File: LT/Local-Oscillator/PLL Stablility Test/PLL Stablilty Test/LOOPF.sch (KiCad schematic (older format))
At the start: 5 parts

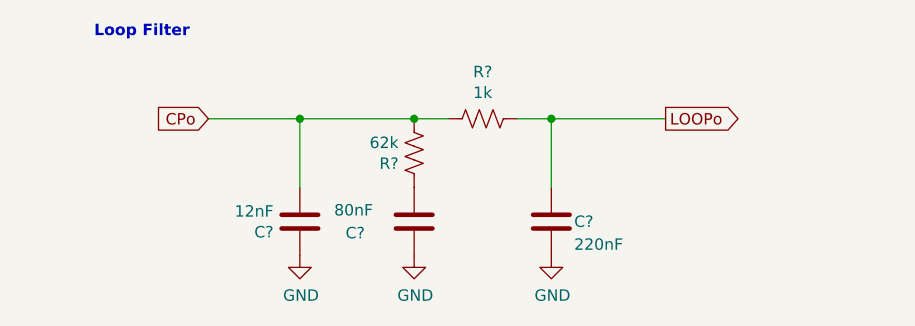
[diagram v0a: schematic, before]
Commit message: completed PLL stability test layour for individual boards
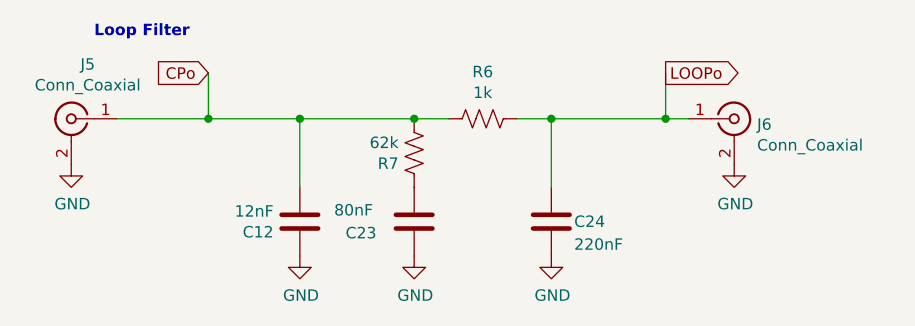
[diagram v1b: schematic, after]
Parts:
- added J5, J6: Conn_Coaxial, Connector_Coaxial:SMA_Molex_73251-1153_EdgeMount_Horizontal, symbol Connector:Conn_Coaxial
- gave numbers to parts that had none: 5
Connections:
- net CPo: now also J5.1 (In)
- net GND: now also J5.2 (Ext), J6.2 (Ext)
- net LOOPo: now also J6.1 (In)
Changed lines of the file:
@@
 AR Path="/5E6F2DE3" Ref="#PWR?"  Part="1"
 AR Path="/5E6E06F1/5E6F2DE3" Ref="#PWR?"  Part="1"
-AR Path="/5E6053F1/5E6F2DE3" Ref="#PWR?"  Part="1"
-F 0 "#PWR?" H 6450 4300 50  0001 C CNN
+AR Path="/5E6053F1/5E6F2DE3" Ref="#PWR0120"  Part="1"
+F 0 "#PWR0120" H 6450 4300 50  0001 C CNN
 F 1 "GND" H 6455 4377 50  0000 C CNN
 F 2 "" H 6450 4550 50  0001 C CNN
@@
 AR Path="/5E6F2DE9" Ref="C?"  Part="1"
 AR Path="/5E6E06F1/5E6F2DE9" Ref="C?"  Part="1"
-AR Path="/5E6053F1/5E6F2DE9" Ref="C?"  Part="1"
-F 0 "C?" H 6550 4400 50  0000 L CNN
+AR Path="/5E6053F1/5E6F2DE9" Ref="C24"  Part="1"
+F 0 "C24" H 6550 4400 50  0000 L CNN
 F 1 "220nF" H 6550 4300 50  0000 L CNN
 F 2 "Capacitor_SMD:C_0805_2012Metric_Pad1.15x1.40mm_HandSolder" H 6488 4250 50  0001 C CNN
@@
 AR Path="/5E6F2DF0" Ref="#PWR?"  Part="1"
 AR Path="/5E6E06F1/5E6F2DF0" Ref="#PWR?"  Part="1"
-AR Path="/5E6053F1/5E6F2DF0" Ref="#PWR?"  Part="1"
-F 0 "#PWR?" H 5850 4300 50  0001 C CNN
+AR Path="/5E6053F1/5E6F2DF0" Ref="#PWR0121"  Part="1"
+F 0 "#PWR0121" H 5850 4300 50  0001 C CNN
 F 1 "GND" H 5855 4377 50  0000 C CNN
 F 2 "" H 5850 4550 50  0001 C CNN
@@
 AR Path="/5E6F2DF7" Ref="C?"  Part="1"
 AR Path="/5E6E06F1/5E6F2DF7" Ref="C?"  Part="1"
-AR Path="/5E6053F1/5E6F2DF7" Ref="C?"  Part="1"
-F 0 "C?" H 5550 4350 50  0000 L CNN
+AR Path="/5E6053F1/5E6F2DF7" Ref="C23"  Part="1"
+F 0 "C23" H 5550 4350 50  0000 L CNN
 F 1 "80nF" H 5500 4450 50  0000 L CNN
 F 2 "Capacitor_SMD:C_0805_2012Metric_Pad1.15x1.40mm_HandSolder" H 5888 4250 50  0001 C CNN
@@
 AR Path="/5E6F2DFD" Ref="#PWR?"  Part="1"
 AR Path="/5E6E06F1/5E6F2DFD" Ref="#PWR?"  Part="1"
-AR Path="/5E6053F1/5E6F2DFD" Ref="#PWR?"  Part="1"
-F 0 "#PWR?" H 5350 4300 50  0001 C CNN
+AR Path="/5E6053F1/5E6F2DFD" Ref="#PWR0122"  Part="1"
+F 0 "#PWR0122" H 5350 4300 50  0001 C CNN
 F 1 "GND" H 5355 4377 50  0000 C CNN
 F 2 "" H 5350 4550 50  0001 C CNN
@@
 AR Path="/5E6F2E04" Ref="C?"  Part="1"
 AR Path="/5E6E06F1/5E6F2E04" Ref="C?"  Part="1"
-AR Path="/5E6053F1/5E6F2E04" Ref="C?"  Part="1"
-F 0 "C?" H 5465 4446 50  0000 L CNN
+AR Path="/5E6053F1/5E6F2E04" Ref="C12"  Part="1"
+F 0 "C12" H 5465 4446 50  0000 L CNN
 F 1 "12nF" H 5465 4355 50  0000 L CNN
 F 2 "Capacitor_SMD:C_0805_2012Metric_Pad1.15x1.40mm_HandSolder" H 5388 4250 50  0001 C CNN
@@
 AR Path="/5E6F2E0B" Ref="R?"  Part="1"
 AR Path="/5E6E06F1/5E6F2E0B" Ref="R?"  Part="1"
-AR Path="/5E6053F1/5E6F2E0B" Ref="R?"  Part="1"
-F 0 "R?" V 5945 3950 50  0000 C CNN
+AR Path="/5E6053F1/5E6F2E0B" Ref="R6"  Part="1"
+F 0 "R6" V 5945 3950 50  0000 C CNN
 F 1 "1k" V 6036 3950 50  0000 C CNN
 F 2 "Resistor_SMD:R_0805_2012Metric_Pad1.15x1.40mm_HandSolder" V 6190 3940 50  0001 C CNN
@@
 AR Path="/5E6F2E11" Ref="R?"  Part="1"
 AR Path="/5E6E06F1/5E6F2E11" Ref="R?"  Part="1"
-AR Path="/5E6053F1/5E6F2E11" Ref="R?"  Part="1"
-F 0 "R?" H 5918 4146 50  0000 L CNN
+AR Path="/5E6053F1/5E6F2E11" Ref="R7"  Part="1"
+F 0 "R7" H 5918 4146 50  0000 L CNN
 F 1 "62k" H 5918 4055 50  0000 L CNN
 F 2 "Resistor_SMD:R_0805_2012Metric_Pad1.15x1.40mm_HandSolder" V 5890 4090 50  0001 C CNN
@@
 Wire Wire Line
 	5850 3950 6000 3950
-Text GLabel 4950 3950 0    50   Input ~ 0
+Text GLabel 4950 3750 0    50   Input ~ 0
 CPo
-Text GLabel 6950 3950 2    50   Output ~ 0
+Text GLabel 6950 3750 2    50   Output ~ 0
 LOOPo
-Wire Wire Line
-	4950 3950 5350 3950
 Wire Wire Line
 	6300 3950 6450 3950
@@
 Connection ~ 6450 3950
 Wire Wire Line
-	6450 3950 6950 3950
-Wire Wire Line
 	5350 4250 5350 3950
 Connection ~ 5350 3950
 Wire Wire Line
 	5350 3950 5850 3950
+$Comp
+L Connector:Conn_Coaxial J5
+U 1 1 5E74812B
+P 4350 3950
+F 0 "J5" H 4278 4188 50  0000 C CNN
+F 1 "Conn_Coaxial" H 4278 4097 50  0000 C CNN
+F 2 "Connector_Coaxial:SMA_Molex_73251-1153_EdgeMount_Horizontal" H 4350 3950 50  0001 C CNN
+F 3 " ~" H 4350 3950 50  0001 C CNN
+	1    4350 3950
+	-1   0    0    -1
+$EndComp
+$Comp
+L Connector:Conn_Coaxial J6
+U 1 1 5E748D0E
+P 7250 3950
+F 0 "J6" H 7350 3925 50  0000 L CNN
+F 1 "Conn_Coaxial" H 7350 3834 50  0000 L CNN
+F 2 "Connector_Coaxial:SMA_Molex_73251-1153_EdgeMount_Horizontal" H 7250 3950 50  0001 C CNN
+F 3 " ~" H 7250 3950 50  0001 C CNN
+	1    7250 3950
+	1    0    0    -1
+$EndComp
+Wire Wire Line
+	6450 3950 6950 3950
+Wire Wire Line
+	4550 3950 4950 3950
+$Comp
+L power:GND #PWR?
+U 1 1 5E749F49
+P 4350 4150
+AR Path="/5E749F49" Ref="#PWR?"  Part="1"
+AR Path="/5E6E06F1/5E749F49" Ref="#PWR?"  Part="1"
+AR Path="/5E6053F1/5E749F49" Ref="#PWR0123"  Part="1"
+F 0 "#PWR0123" H 4350 3900 50  0001 C CNN
+F 1 "GND" H 4355 3977 50  0000 C CNN
+F 2 "" H 4350 4150 50  0001 C CNN
+F 3 "" H 4350 4150 50  0001 C CNN
+	1    4350 4150
+	1    0    0    -1
+$EndComp
+$Comp
+L power:GND #PWR?
+U 1 1 5E74A2B4
+P 7250 4150
+AR Path="/5E74A2B4" Ref="#PWR?"  Part="1"
+AR Path="/5E6E06F1/5E74A2B4" Ref="#PWR?"  Part="1"
+AR Path="/5E6053F1/5E74A2B4" Ref="#PWR0124"  Part="1"
+F 0 "#PWR0124" H 7250 3900 50  0001 C CNN
+F 1 "GND" H 7255 3977 50  0000 C CNN
+F 2 "" H 7250 4150 50  0001 C CNN
+F 3 "" H 7250 4150 50  0001 C CNN
+	1    7250 4150
+	1    0    0    -1
+$EndComp
+Wire Wire Line
+	4950 3750 4950 3950
+Connection ~ 4950 3950
+Wire Wire Line
+	4950 3950 5350 3950
+Wire Wire Line
+	6950 3750 6950 3950
+Connection ~ 6950 3950
+Wire Wire Line
+	6950 3950 7050 3950
 $EndSCHEMATC
